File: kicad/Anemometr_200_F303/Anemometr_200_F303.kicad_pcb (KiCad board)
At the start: 2 copper layers, 25.8 x 45.3 mm, 51 parts, among them J1 Conn_01x01_Female, J10 USB_B_Micro, J11 Conn_01x01_Female, J12 Conn_01x01_Female, J13 Conn_01x01_Female, J14 Conn_01x01_Female, J15 Conn_01x01_Female, J16 Conn_01x01_Female, J17 Conn_01x01_Female, J18 Conn_01x01_Female, J19 Conn_01x01_Female, J2 Conn_01x01_Female, J20 Conn_01x01_Female, J21 Conn_01x01_Female, J22 Conn_01x01_Female, J23 Conn_01x01_Female, J24 Conn_01x01_Female, J25 Conn_01x01_Female, J26 Conn_01x01_Female, J27 Conn_01x01_Female, J28 Conn_01x01_Female, J29 Conn_01x01_Female, J3 Conn_01x01_Female, J30 Conn_01x01_Female, J31 Conn_01x01_Female, J32 Conn_01x01_Female, J4 Conn_01x01_Female, J5 Conn_01x01_Female, J6 Conn_01x01_Female, J7 Conn_01x01_Female, J8 Conn_01x01_Female, J9 Conn_01x01_Female, U1 AP1117-33, U2 STM32F303CCTx, U3 CH340C, Y1 16MHz

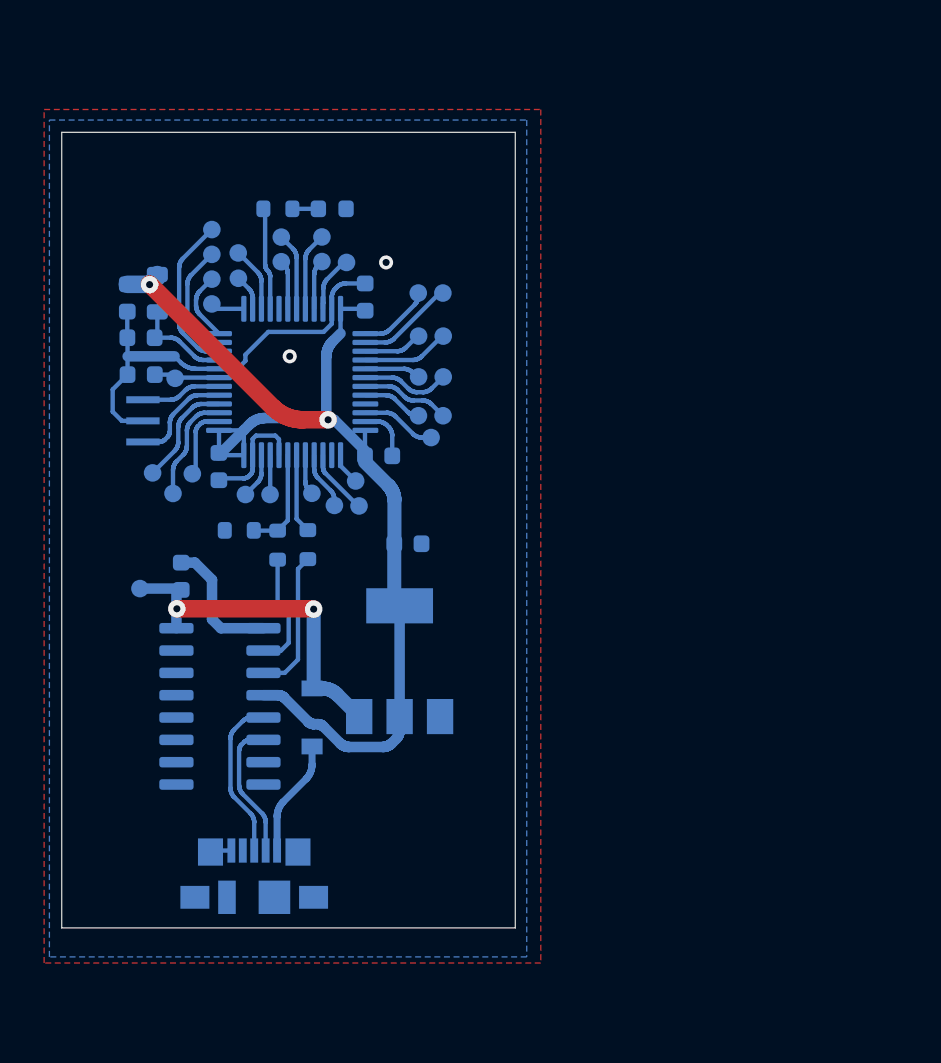
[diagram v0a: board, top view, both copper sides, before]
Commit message: изменено:      kicad/Amp200_2/Amp200-cache.lib 	изменено:      kicad/Amp200_2/Amp200.kicad_pcb 	изменено:      kicad/Amp200_2/Amp200.kicad_pcb-bak 	изменено:      kicad/Amp200_2/Amp200.sch 	изменено:      kicad/Amp200_2/Amp200.sch-bak 	изменено:      kicad/Amp200_2/fp-info-cache 	изменено:      kicad/Anemometr_200_F303/Anemometr_200_F303.kicad_pcb 	изменено:      kicad/Anemometr_200_F303/Anemometr_200_F303.kicad_pcb-bak 	изменено:      kicad/Anemometr_200_F303/Anemometr_200_F303.sch 	изменено:      kicad/Anemometr_200_F303/Anemometr_200_F303.sch-bak 	изменено:      stm32cubeide/Anemometer_200_F303/.cproject 	изменено:      stm32cubeide/Anemometer_200_F303/.mxproject 	изменено:      stm32cubeide/Anemometer_200_F303/.settings/language.settings.xml 	изменено:      stm32cubeide/Anemometer_200_F303/.settings/stm32cubeide.project.prefs 	изменено:      stm32cubeide/Anemometer_200_F303/Anemometer_200_F303.ioc 	изменено:      stm32cubeide/Anemometer_200_F303/Anemometer_200_F303.launch 	изменено:      stm32cubeide/Anemometer_200_F303/Core/Inc/main.h 	изменено:      stm32cubeide/Anemometer_200_F303/Core/Inc/stm32f3xx_hal_conf.h 	изменено:      stm32cubeide/Anemometer_200_F303/Core/Inc/stm32f3xx_it.h 	изменено:      stm32cubeide/Anemometer_200_F303/Core/Src/main.c 	изменено:      stm32cubeide/Anemometer_200_F303/Core/Src/stm32f3xx_hal_msp.c 	изменено:      stm32cubeide/Anemometer_200_F303/Core/Src/stm32f3xx_it.c 	удалено:       stm32cubeide/Anemometer_200_F303/Debug/Anemometer_200_F303.bin 	изменено:      stm32cubeide/Anemometer_200_F303/Debug/Anemometer_200_F303.elf 	изменено:      stm32cubeide/Anemometer_200_F303/Debug/Anemometer_200_F303.list 	изменено:      stm32cubeide/Anemometer_200_F303/Debug/Anemometer_200_F303.map 	изменено:      stm32cubeide/Anemometer_200_F303/Debug/Core/Src/main.d 	изменено:      stm32cubeide/Anemometer_200_F303/Debug/Core/Src/main.o 	изменено:      stm32cubeide/Anemometer_200_F303/Debug/Core/Src/main.su 	изменено:      stm32cubeide/Anemometer_200_F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
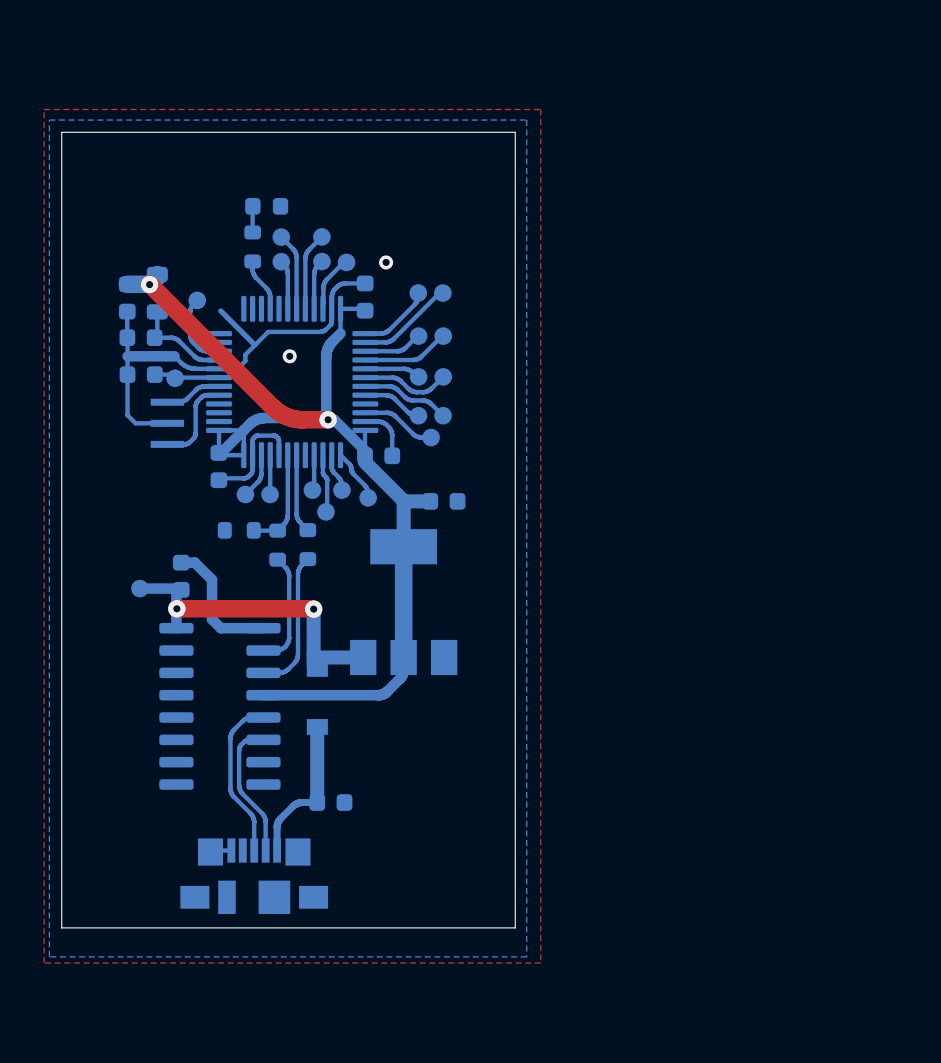
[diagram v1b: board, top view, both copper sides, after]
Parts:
- removed J28, J29, J30, J31, J32, J7, J8, J9: Conn_01x01_Female, My-library:mini_conn
- added C9: C, Capacitor_SMD:C_0603_1608Metric, B.Cu at (46.8, 81.8)
- moved J5 15.3 mm to (47.4, 64.1)
- moved J3 4.11 mm to (39.2, 53.3)
- moved D1 3.73 mm to (43.1, 47.9)
- moved U1 3.37 mm to (50.9, 70.5)
- moved C1 3.16 mm to (53.2, 64.7)
- moved R1 2.60 mm to (42.3, 50.2), turned to 270 degrees
- moved J26 1.91 mm to (46.5, 65.3)
- moved J25 1.52 mm to (45.7, 64.1)
- moved Y1 1.40 mm to (37.5, 60.3)
- moved J23 1.19 mm to (48.9, 64.5)
- moved D2 1.15 mm to (46.0, 75.9)
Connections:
- J5 pad 1: /AnIn2 -> /zero
- U2 pad 11: /AnIn2 -> (no net)
- U2 pad 12: /AnIn3 -> (no net)
- U2 pad 13: /AnIn4 -> (no net)
- U2 pad 14: /Inc -> (no net)
- U2 pad 15: /U-D -> (no net)
- U2 pad 2: /CS1 -> (no net)
- U2 pad 3: /CS2 -> (no net)
- U2 pad 38: (no net) -> /zero
- U2 pad 4: /CS3 -> (no net)
- U2 pad 41: /CS4 -> (no net)
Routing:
- net /AnIn2: track 6.74 -> 0.00 mm
- net /CS2: track 6.19 -> 0.00 mm
- net /CS3: track 6.16 -> 0.00 mm
- net /AnIn1: track 9.14 -> 4.23 mm
- net /CS1: track 4.10 -> 0.00 mm
- net /AnIn3: track 3.95 -> 0.00 mm
- net /U-D: track 3.70 -> 0.00 mm
- net GND: track 43.3 -> 46.4 mm
- net Net-(R1-Pad2): track 5.81 -> 3.04 mm
- net +3V3: track 67.2 -> 64.7 mm
- net /CS4: track 2.29 -> 0.00 mm
- net /zero: track 0.00 -> 2.18 mm
- net /Inc: track 2.04 -> 0.00 mm
- net Net-(C9-Pad1): track 6.64 -> 8.60 mm
- net /AnIn4: track 1.93 -> 0.00 mm
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
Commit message: изменено:      Documents/matLab/convData.m 	изменено:      kicad/Anemometr_200_F303/Anemometr_200_F303-cache.lib 	изменено:      kicad/Anemometr_200_F303/Anemometr_200_F303.kicad_pcb 	изменено:      kicad/Anemometr_200_F303/Anemometr_200_F303.kicad_pcb-bak 	изменено:      kicad/Anemometr_200_F303/Anemometr_200_F303.sch 	изменено:      kicad/Anemometr_200_F303/Anemometr_200_F303.sch-bak 	изменено:      kicad/Anemometr_200_F303/fp-info-cache 	изменено:      stm32cubeide/Anemometer_200_F303/Anemometer_200_F303.ioc 	новый файл:    stm32cubeide/Anemometer_200_F303/Core/Inc/FFTImplementationCallback.h 	изменено:      stm32cubeide/Anemometer_200_F303/Core/Inc/main.h 	новый файл:    stm32cubeide/Anemometer_200_F303/Core/Inc/maxEnvHilbert.h 	новый файл:    stm32cubeide/Anemometer_200_F303/Core/Inc/maxEnvHilbert_data.h 	новый файл:    stm32cubeide/Anemometer_200_F303/Core/Inc/maxEnvHilbert_terminate.h 	новый файл:    stm32cubeide/Anemometer_200_F303/Core/Inc/rt_nonfinite.h 	новый файл:    stm32cubeide/Anemometer_200_F303/Core/Inc/rtwtypes.h 	новый файл:    stm32cubeide/Anemometer_200_F303/Core/Inc/tmwtypes.h 	новый файл:    stm32cubeide/Anemometer_200_F303/Core/Src/FFTImplementationCallback.c 	изменено:      stm32cubeide/Anemometer_200_F303/Core/Src/main.c 	новый файл:    stm32cubeide/Anemometer_200_F303/Core/Src/maxEnvHilbert.c 	новый файл:    stm32cubeide/Anemometer_200_F303/Core/Src/maxEnvHilbert_data.c 	новый файл:    stm32cubeide/Anemometer_200_F303/Core/Src/maxEnvHilbert_terminate.c 	новый файл:    stm32cubeide/Anemometer_200_F303/Core/Src/rt_nonfinite.c 	изменено:      stm32cubeide/Anemometer_200_F303/Core/Src/stm32f3xx_hal_msp.c 	изменено:      stm32cubeide/Anemometer_200_F303/Core/Src/stm32f3xx_it.c 	изменено:      stm32cubeide/Anemometer_200_F303/Debug/Anemometer_200_F303.elf 	изменено:      stm32cubeide/Anemometer_200_F303/Debug/Anemometer_200_F303.list 	изменено:      stm32cubeide/Anemometer_200_F303/Debug/Anemometer_200_F303.map 	изменено:      stm32cubeide/Anemo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
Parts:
- removed J18, J20, J21, J22, J24: Conn_01x01_Female, My-library:mini_conn
- added C10: C, Capacitor_SMD:C_0402_1005Metric, F.Cu at (65.3, 50.3)
- added C11: C, Capacitor_SMD:C_0402_1005Metric, F.Cu at (59.7, 50.3)
- added C12: C, Capacitor_SMD:C_0603_1608Metric, F.Cu at (56.2, 61.2)
- added C13: C, Capacitor_SMD:C_0402_1005Metric, B.Cu at (63.5, 60.0)
- added C14: 10n, Capacitor_SMD:C_0402_1005Metric, F.Cu at (69.3, 57.9)
- added C15: 4.7u, Capacitor_SMD:C_0402_1005Metric, F.Cu at (69.3, 59.0)
- added C16: 100n, Capacitor_SMD:C_0805_2012Metric, F.Cu at (45.2, 79.7)
- added C17: C, Capacitor_SMD:C_0805_2012Metric, F.Cu at (50.9, 79.7)
- added C18: C, Capacitor_SMD:C_0805_2012Metric, F.Cu at (53.0, 79.7)
- added C19: 22n, Capacitor_SMD:C_0402_1005Metric, F.Cu at (65.8, 69.5)
- added C20: 6.8n, Capacitor_SMD:C_0402_1005Metric, F.Cu at (62.6, 68.0)
- added C21: 6.8n, Capacitor_SMD:C_0402_1005Metric, F.Cu at (59.4, 68.0)
- added C22: 10n, Capacitor_SMD:C_0402_1005Metric, F.Cu at (62.0, 69.6)
- added C23: C, Capacitor_SMD:C_0402_1005Metric, B.Cu at (61.1, 60.0)
- added C24: C, Capacitor_SMD:C_0402_1005Metric, F.Cu at (69.3, 61.9)
- added C25: C, Capacitor_SMD:C_0402_1005Metric, B.Cu at (65.8, 60.0)
- added C26: C, Capacitor_SMD:C_0402_1005Metric, F.Cu at (69.3, 60.5)
- added C27: C, Capacitor_SMD:C_0402_1005Metric, F.Cu at (64.7, 52.6)
- added C28: 1000, Capacitor_Tantalum_SMD:CP_EIA-7343-15_Kemet-W, F.Cu at (38.8, 74.1)
- added C29: CP, Capacitor_Tantalum_SMD:CP_EIA-7343-15_Kemet-W, F.Cu at (65.2, 85.1)
- added C30: C, Capacitor_SMD:C_0805_2012Metric, B.Cu at (55.6, 72.9)
- added C31: 6.8n, Capacitor_SMD:C_0402_1005Metric, F.Cu at (66.7, 46.7)
- added C32: 6.8n, Capacitor_SMD:C_0402_1005Metric, F.Cu at (66.7, 45.4)
- added C33: 6.8n, Capacitor_SMD:C_0402_1005Metric, F.Cu at (66.7, 44.2)
- added C34: 6.8n, Capacitor_SMD:C_0402_1005Metric, F.Cu at (66.7, 42.8)
- added C35: 6.8n, Capacitor_SMD:C_1206_3216Metric, F.Cu at (62.7, 43.3)
- added D3: LED, LED_SMD:LED_0603_1608Metric, F.Cu at (67.9, 51.6)
- added D4: LED, LED_SMD:LED_0603_1608Metric, F.Cu at (67.9, 53.2)
- added D5: LMR50410, Package_TO_SOT_SMD:SOT-23-6, F.Cu at (48.0, 79.7)
- added D6: H1102NL, My-library:H1102N, B.Cu at (63.2, 59.6)
- added D7: RT9400, My-library:TR9400, F.Cu at (71.4, 52.2)
- added D8: LED, LED_SMD:LED_0603_1608Metric, B.Cu at (54.0, 75.7)
- added J7: Conn_01x08, Connector_JST:JST_SH_BM08B-SRSS-TB_1x08-1MP_P1.00mm_Vertical, B.Cu at (61.6, 50.9)
- added L2: L, Inductor_SMD:L_0805_2012Metric, F.Cu at (54.8, 59.4)
- added L3: 4.7u, Inductor_SMD:L_Abracon_ASPI-0630LR, F.Cu at (48.8, 74.0)
- added R10: 22.1k, Resistor_SMD:R_0603_1608Metric, F.Cu at (48.1, 82.7)
- added R11: 49R9, Resistor_SMD:R_0402_1005Metric, F.Cu at (65.2, 67.9)
- added R12: 49R9, Resistor_SMD:R_0402_1005Metric, F.Cu at (67.4, 67.9)
- added R13: 10R, Resistor_SMD:R_0402_1005Metric, F.Cu at (66.3, 67.9)
- added R14: 82R, Resistor_SMD:R_0402_1005Metric, F.Cu at (61.6, 68.0)
- added R15: 82R, Resistor_SMD:R_0402_1005Metric, F.Cu at (60.5, 68.0)
- added R16: 1k, Resistor_SMD:R_0603_1608Metric, B.Cu at (51.2, 75.7)
- added R17: 75, Resistor_SMD:R_0402_1005Metric, F.Cu at (68.8, 46.7)
- added R18: 75, Resistor_SMD:R_0402_1005Metric, F.Cu at (68.7, 45.4)
- added R19: 75, Resistor_SMD:R_0402_1005Metric, F.Cu at (68.7, 44.1)
- added R20: 75, Resistor_SMD:R_0402_1005Metric, F.Cu at (68.6, 42.8)
- added R3: 1M, Resistor_SMD:R_0402_1005Metric, F.Cu at (62.5, 52.5)
- added R6: 1M, Resistor_SMD:R_0402_1005Metric, F.Cu at (67.3, 55.6)
- added R7: 1M, Resistor_SMD:R_0402_1005Metric, F.Cu at (67.3, 54.5)
- added R8: 12.4k, Resistor_SMD:R_0402_1005Metric, F.Cu at (64.2, 66.1)
- added R9: 88.7k, Resistor_SMD:R_0603_1608Metric, F.Cu at (51.2, 82.7)
- added U4: W5500, Package_QFP:LQFP-48_7x7mm_P0.5mm, F.Cu at (62.4, 59.7)
- added Y2: Crystal_GND24_Small, Crystal:Crystal_SMD_SeikoEpson_FA238-4Pin_3.2x2.5mm, F.Cu at (62.5, 50.2)
- moved J10 4.98 mm to (41.5, 90.9)
- moved C9 1.96 mm to (46.8, 83.8)
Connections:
- net Net-(C2-Pad1) renamed +5v
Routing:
- net GND: track 46.4 -> 193.3 mm, vias 2 -> 6
- net +3.3VA: track 0.00 -> 41.4 mm, vias 0 -> 3
- net +24v: track 0.00 -> 38.2 mm, vias 0 -> 1
- net +3V3: track 64.7 -> 100.9 mm, vias 2 -> 3
- net Net-(D6-Pad1): track 0.00 -> 26.4 mm, vias 0 -> 2
- net Net-(D6-Pad10): track 0.00 -> 22.4 mm
- net Net-(D7-Pad1): track 0.00 -> 22.2 mm
- net Net-(D6-Pad3): track 0.00 -> 20.9 mm, vias 0 -> 2
- net +5v: track 19.0 -> 38.3 mm
- net Net-(D7-Pad2): track 0.00 -> 18.6 mm
- net Net-(D6-Pad15): track 0.00 -> 16.8 mm
- net /NSS: track 4.17 -> 20.5 mm, vias 0 -> 1
- net /EthRST: track 3.25 -> 17.0 mm, vias 0 -> 1
- net /MISO: track 3.38 -> 16.3 mm, vias 0 -> 1
- net /SCK: track 5.54 -> 18.4 mm, vias 0 -> 1
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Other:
- board size 25.8 x 45.3 mm -> 46.1 x 54.3 mm
